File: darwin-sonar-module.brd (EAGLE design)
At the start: 85 x 25 mm, 19 parts, among them J1 2X6-HEADERS, J2 95501-6889VERT, U3 M24C02-WMN6TP, U4 PCA9615

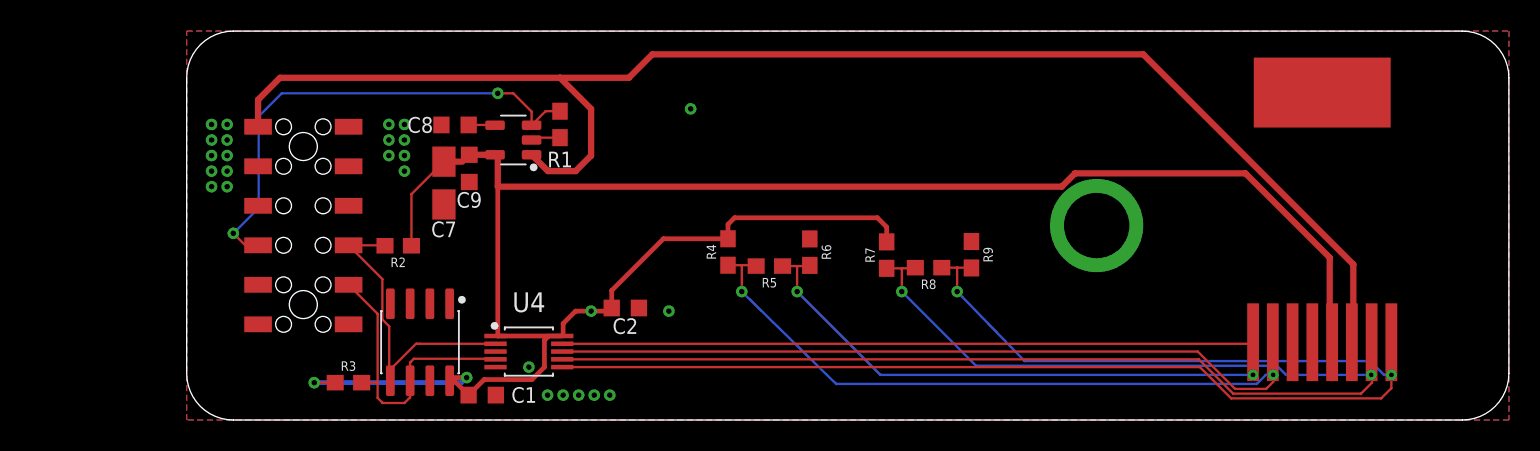
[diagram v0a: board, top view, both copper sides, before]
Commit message: Migrated to new footprint and added icon.
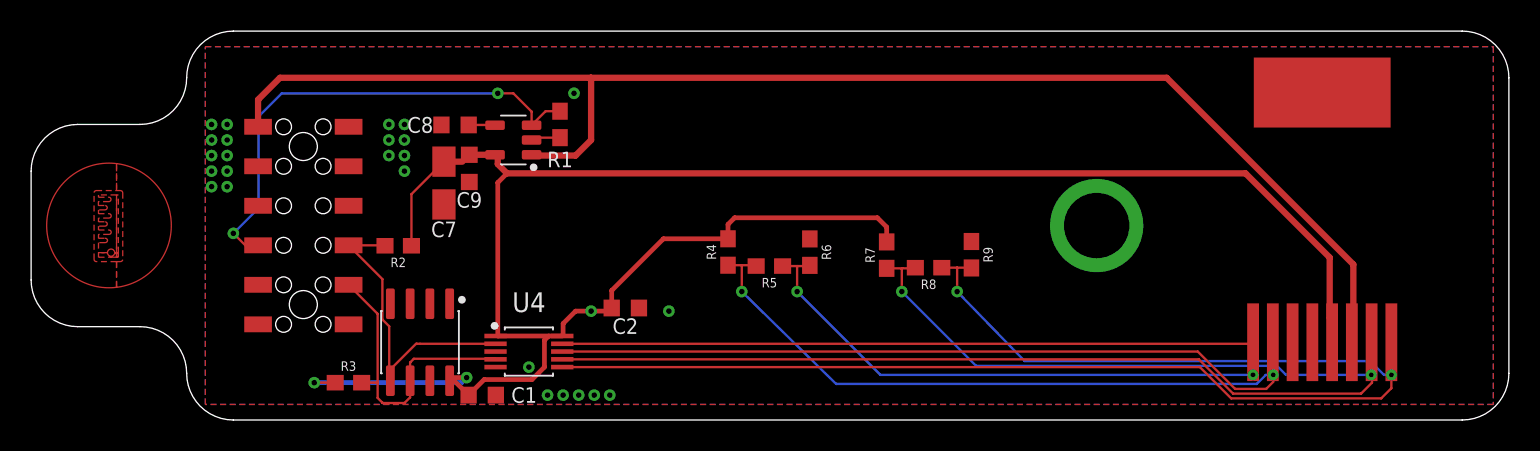
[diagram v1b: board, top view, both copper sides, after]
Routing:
- net UNREG: track 94.5 -> 91.0 mm
- added copper zone on layer 1, net GND1
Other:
- board size 85 x 25 mm -> 95 x 25 mm
- board text added: "THIS SIDE DOWN"
